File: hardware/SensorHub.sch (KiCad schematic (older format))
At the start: 39 parts, among them IC1 VEML6070, IC2 LT3652EMSE, IC3 BME680, IC4 BH1726, IC5 MCP9808, M1 ParticleArgon, SW1 ENABLE, X1 WIND, X2 SOLAR

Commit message: Clean up hardware files
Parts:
- removed C1: 1uF, Capacitor_SMD:C_0805_2012Metric_Pad1.15x1.40mm_HandSolder, symbol Device:C
- IC3: Order Number 262-BME680 -> 262-BME680
- IC5: Mouser (none) -> 579-MCP9808T-E/MS
- RV1: Mfr. No. TS53YJ103MR10 -> TS53YJ103MR10
- SW1: Distributor (none) -> Mouser; Mfr. No. A6S-1104-PH -> A6S-1104-PH
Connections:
- net GND: now also IC2.6 (TIMER)
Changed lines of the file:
@@
 F 5 "BMP680" H 11121 2509 50  0001 R CNN "Mfr. No."
 F 6 "Mouser" H 11550 2600 50  0001 C CNN "Distributor"
-F 7 "262-BME680 " H 11550 2600 50  0001 C CNN "Order Number"
+F 7 "262-BME680" H 11550 2600 50  0001 C CNN "Order Number"
 	1    11550 2600
 	1    0    0    -1
@@
 F 4 "Microchip" H 9500 2650 50  0001 C CNN "Mfr."
 F 5 "MCP9808T-E/MS " H 9500 2650 50  0001 C CNN "Mfr. No."
-F 6 "" H 9500 2650 50  0001 C CNN "Mouser"
+F 6 "579-MCP9808T-E/MS " H 9500 2650 50  0001 C CNN "Mouser"
 F 7 "Mouser" H 9500 2650 50  0001 C CNN "Distributor"
 F 8 "579-MCP9808T-E/MS " H 9500 2650 50  0001 C CNN "Order Number"
@@
 F 3 "~" H 9250 6500 50  0001 C CNN
 F 4 "Omron" H 9250 6857 50  0001 C CNN "Mfr."
-F 5 "A6S-1104-PH " H 9250 6766 50  0001 C CNN "Mfr. No."
+F 5 "A6S-1104-PH" H 9250 6766 50  0001 C CNN "Mfr. No."
 F 6 "653-A6S1104PH" H 9250 6500 50  0001 C CNN "Order Number"
+F 7 "Mouser" H 9250 6500 50  0001 C CNN "Distributor"
 	1    9250 6500
 	1    0    0    -1
@@
 F 1 "10k" V 1750 2350 50  0000 R CNN
 F 2 "Potentiometer_SMD_Kampi:Potentiometer_Vishay_TS53YJ_Vertical" H 1850 2300 50  0001 C CNN
-F 3 "~" H 1850 2300 50  0001 C CNN
+F 3 "https://www.mouser.de/datasheet/2/427/ts53-1763731.pdf" H 1850 2300 50  0001 C CNN
 F 4 "Vishay" H 1780 2300 50  0001 R CNN "Mfr."
-F 5 "TS53YJ103MR10 " H 1780 2391 50  0001 R CNN "Mfr. No."
+F 5 "TS53YJ103MR10" H 1780 2391 50  0001 R CNN "Mfr. No."
 F 6 "Mouser" H 1850 2300 50  0001 C CNN "Distributor"
 F 7 "72-TS53YJ-10K " H 1850 2300 50  0001 C CNN "Order Number"
@@
 $EndComp
 Wire Wire Line
-	1850 4100 1850 4200
-Wire Wire Line
 	1850 4200 2400 4200
 Connection ~ 2400 4200
@@
 Wire Wire Line
 	1900 3600 1850 3600
-Wire Wire Line
-	1850 3600 1850 3800
 $Comp
 L Device:R R4
@@
 	1    1600 8575
 	1    0    0    1
-$EndComp
-$Comp
-L Device:C C1
-U 1 1 5EE01B4B
-P 1850 3950
-F 0 "C1" H 1965 3996 50  0000 L CNN
-F 1 "1uF" H 1965 3905 50  0000 L CNN
-F 2 "Capacitor_SMD:C_0805_2012Metric_Pad1.15x1.40mm_HandSolder" H 1888 3800 50  0001 C CNN
-F 3 "~" H 1850 3950 50  0001 C CNN
-F 4 "Kemet" H 1850 3950 50  0001 C CNN "Mfr."
-F 5 "C0805X105K3RAC3316" H 1850 3950 50  0001 C CNN "Mfr. No."
-F 6 "Mouser" H 1850 3950 50  0001 C CNN "Distributor"
-F 7 "80-C0805X105K3R3316" H 1850 3950 50  0001 C CNN "Order Number"
-	1    1850 3950
-	-1   0    0    1
 $EndComp
 $Comp
@@
 Text Notes 5450 6300 0    50   ~ 0
 The voltage divider is designed\nfor a 17.8 V solar panel.
+Wire Wire Line
+	1850 3600 1850 4200
 $EndSCHEMATC

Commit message: Init branch
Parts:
- L1: value 68uH -> 33uH; Mfr. No. IDC2512ER680M -> IDC2512ER330M; Order Number 70-IDC2512ER680M -> 70-IDC2512ER330M
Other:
- note added: "- Set the voltage at the SET testpoint to >2.7 V in maximum sun."
- note removed: "- Adjust R8 to increase or decrease the maximum charge current."
- note removed: "- Set the voltage at the SET testpoint to 2.8 V in maximum sun."
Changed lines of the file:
@@
 	1    0    0    -1
 $EndComp
-Wire Wire Line
-	2400 3800 2400 4200
 $Comp
 L Device:R_POT RV1
@@
 $EndComp
 Wire Wire Line
-	1850 4200 2400 4200
-Connection ~ 2400 4200
-Wire Wire Line
-	2400 4200 2400 4350
-Wire Wire Line
 	1900 3600 1850 3600
 $Comp
@@
 $EndComp
 Wire Wire Line
-	2400 4200 3050 4200
-Wire Wire Line
 	3650 4200 3650 4100
 Wire Wire Line
@@
 P 3700 2650
 F 0 "L1" V 3775 2650 50  0000 C CNN
-F 1 "68uH" V 3850 2650 50  0000 C CNN
+F 1 "33uH" V 3850 2650 50  0000 C CNN
 F 2 "Inductor_SMD:L_2512_6332Metric_Pad1.52x3.35mm_HandSolder" H 3700 2650 50  0001 C CNN
-F 3 "~" H 3700 2650 50  0001 C CNN
+F 3 "https://www.mouser.de/datasheet/2/427/idc2512-1762893.pdf" H 3700 2650 50  0001 C CNN
 F 4 "Vishay / Dale" V 3981 2650 50  0001 C CNN "Mfr."
-F 5 "IDC2512ER680M" V 3890 2650 50  0001 C CNN "Mfr. No."
+F 5 "IDC2512ER330M" V 3890 2650 50  0001 C CNN "Mfr. No."
 F 6 "Mouser" H 3700 2650 50  0001 C CNN "Distributor"
-F 7 "70-IDC2512ER680M" H 3700 2650 50  0001 C CNN "Order Number"
+F 7 "70-IDC2512ER330M" H 3700 2650 50  0001 C CNN "Order Number"
 	1    3700 2650
 	0    1    1    0
@@
 Wire Wire Line
 	3050 4100 3050 4200
-Connection ~ 3050 4200
-Wire Wire Line
-	3050 4200 3650 4200
+Wire Wire Line
+	3050 4200 3350 4200
 $Comp
 L Battery_Management:LT3652EMSE IC2
@@
 - Connect NTC with battery pack (optional).\n
 Text Notes 750  750  0    50   ~ 0
-- Set the voltage at the SET testpoint to 2.8 V in maximum sun.
-Text Notes 750  1050 0    50   ~ 0
-- Adjust R8 to increase or decrease the maximum charge current.
+- Set the voltage at the SET testpoint to >2.7 V in maximum sun.
 Text Notes 775  10100 0    100  ~ 20
 Device
@@
 Wire Wire Line
 	9900 2650 10100 2650
+Text Notes 750  1050 0    50   ~ 0
+- The device is powered by an external solar panel with a minimum output power of 2 W and a voltage from 6 V to 20 V.
 Text Notes 750  1200 0    50   ~ 0
-- The device is powered by an external solar panel with a minimum output power of 2 W and a voltage from 6 V to 20 V.
-Text Notes 750  1350 0    50   ~ 0
 - Interface for a Davis Anemometer for wind speed and wind direction measurement.
 NoConn ~ 8800 7000
@@
 Text Notes 5450 6300 0    50   ~ 0
 The voltage divider is designed\nfor a 17.8 V solar panel.
-Wire Wire Line
-	1850 3600 1850 4200
+$Comp
+L power:GND #PWR?
+U 1 1 5F0D963C
+P 1850 4350
+F 0 "#PWR?" H 1850 4100 50  0001 C CNN
+F 1 "GND" H 1855 4177 50  0000 C CNN
+F 2 "" H 1850 4350 50  0001 C CNN
+F 3 "" H 1850 4350 50  0001 C CNN
+	1    1850 4350
+	1    0    0    -1
+$EndComp
+Wire Wire Line
+	1850 3600 1850 4350
+$Comp
+L power:GND #PWR?
+U 1 1 5F0EDDBF
+P 3350 4350
+F 0 "#PWR?" H 3350 4100 50  0001 C CNN
+F 1 "GND" H 3355 4177 50  0000 C CNN
+F 2 "" H 3350 4350 50  0001 C CNN
+F 3 "" H 3350 4350 50  0001 C CNN
+	1    3350 4350
+	1    0    0    -1
+$EndComp
+Wire Wire Line
+	3350 4350 3350 4200
+Connection ~ 3350 4200
+Wire Wire Line
+	3350 4200 3650 4200
+Wire Wire Line
+	2400 3800 2400 4350
 $EndSCHEMATC

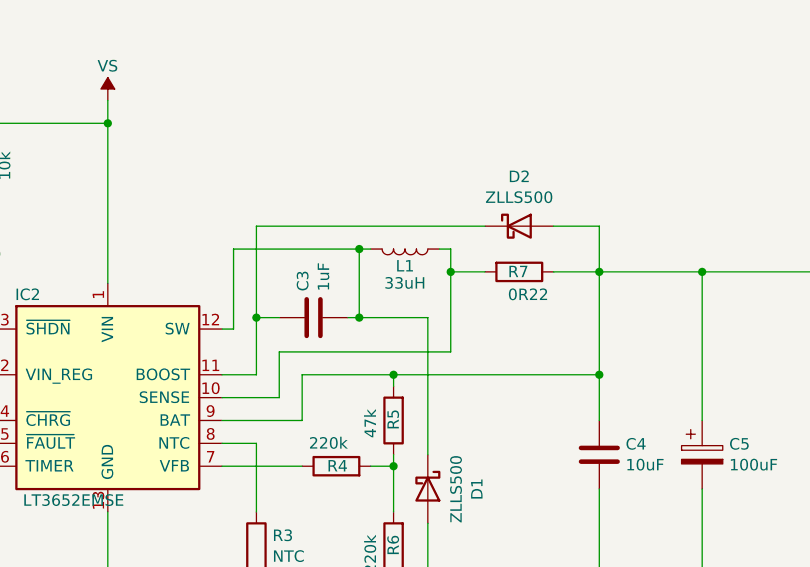
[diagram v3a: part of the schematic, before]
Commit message: Update README, BOM and schematics
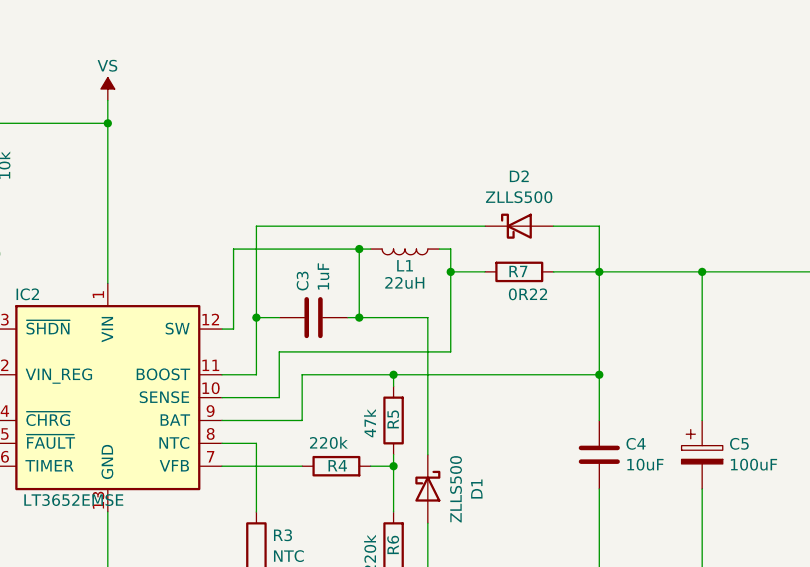
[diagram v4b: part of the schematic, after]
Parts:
- L1: value 33uH -> 22uH
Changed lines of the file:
@@
 F 1 "ZLLS500" H 4200 2675 50  0000 C CNN
 F 2 "Diode_SMD:D_SOT-23_ANK" H 4200 2550 50  0001 C CNN
-F 3 "~" H 4200 2550 50  0001 C CNN
+F 3 "https://www.diodes.com/assets/Datasheets/ZLLS500.pdf" H 4200 2550 50  0001 C CNN
 F 4 "Diodes Incorporated" H 4200 2550 50  0001 C CNN "Mfr."
 F 5 "ZLLS500TA" H 4200 2550 50  0001 C CNN "Mfr. No."
@@
 P 3700 2650
 F 0 "L1" V 3775 2650 50  0000 C CNN
-F 1 "33uH" V 3850 2650 50  0000 C CNN
+F 1 "22uH" V 3850 2650 50  0000 C CNN
 F 2 "Inductor_SMD:L_2512_6332Metric_Pad1.52x3.35mm_HandSolder" H 3700 2650 50  0001 C CNN
 F 3 "https://www.mouser.de/datasheet/2/427/idc2512-1762893.pdf" H 3700 2650 50  0001 C CNN
@@
 F 1 "ZLLS500" H 3800 3825 50  0000 C CNN
 F 2 "Diode_SMD:D_SOT-23_ANK" H 3800 3700 50  0001 C CNN
-F 3 "~" H 3800 3700 50  0001 C CNN
+F 3 "https://www.diodes.com/assets/Datasheets/ZLLS500.pdf" H 3800 3700 50  0001 C CNN
 F 4 "Diodes Incorporated" H 3800 3700 50  0001 C CNN "Mfr."
 F 5 "ZLLS500TA" H 3800 3700 50  0001 C CNN "Mfr. No."
